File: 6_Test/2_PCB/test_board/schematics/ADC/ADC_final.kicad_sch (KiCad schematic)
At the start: 19 parts, among them J3 TSW-107-07-F-D, J4 TSW-107-07-F-D

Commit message: Edits 112524
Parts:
- removed J?: 6130XX21121_61302021121, 6130XX21121_61302021121:61302021121, symbol 2x10Header:6130XX21121_61302021121
- removed R30, R31, R32, R33, R34: 1k, symbol Device:R_US
- added C11, C13, C15: 4.7u, Cap4.7uFFootprints:CAP_0603_CL10A_1P6XP8_SAM, symbol Device:C
- added C12, C14, C16: 100n, cap100nFFootprints:CAP_CL05_SAM, symbol Device:C
- added J10: Chip_AVSS_GND_Jumpers, ECE628_lib:6x2header, symbol 6x2Header:TSW-107-07-F-D
- added J5: Chip_VDD_Jumpers, Connector_PinHeader_2.54mm:PinHeader_2x03_P2.54mm_Vertical, symbol Connector_Generic:Conn_02x03_Odd_Even
- added R11, R12, R13, R14, R15: 1k, resistor1kFootprints:RC0402N_YAG, symbol Device:R_US
- ADC2: value ~ -> ADC_Socket; footprint Package_DFN_QFN:QFN-32-1EP_5x5mm_P0.5mm_EP3.1x3.1mm_ThermalVias -> Package_DIP:DIP-32_W15.24mm_Socket
- ADC?: value ~ -> ADC_Chip
- C17: renamed from C13; footprint (none) -> cap100pFFootprints:G-033_MUR
- C18: renamed from C14; footprint (none) -> cap100pFFootprints:G-033_MUR
- C19: renamed from C15; footprint (none) -> cap100pFFootprints:G-033_MUR
- C20: renamed from C16; footprint (none) -> cap100pFFootprints:G-033_MUR
- C21: renamed from C17; footprint (none) -> cap100pFFootprints:G-033_MUR
- C22: renamed from C18; footprint (none) -> cap100pFFootprints:G-033_MUR
- J6: renamed from J?; value ~ -> BNC_Odd; footprint (none) -> ECE628_lib:bnc_mini_gnd
- J7: renamed from J?; value ~ -> BNC_Even; footprint (none) -> ECE628_lib:bnc_mini_gnd
- J8: renamed from J3; value TSW-107-07-F-D -> BNC_Jumpers
- J9: renamed from J4; value TSW-107-07-F-D -> Analog_Input_Jumpers
- R10: renamed from R29; footprint (none) -> resistor1kFootprints:RC0402N_YAG
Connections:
- net AVSS: now also J10.1, J10.2, J10.3
- net GND: now also C11.2, C12.2, C13.2, C14.2, C15.2, C16.2, J10.12, J10.4, J10.5, J10.6
- net IN2: now also R11.1
- net IN3: now also R12.1
- net IN4: now also R13.1
- net IN5: now also R14.1
- net IN6: now also R15.1
- net IOVDD: now also J5.3 (Pin_3), J5.5 (Pin_5)
- net VDD: now also J5.1 (Pin_1)
- net at ADC2.7 (IN5), ADC?.7 (IN5), C21.1: now also R14.2
- net at ADC2.2 (IN2), ADC?.2 (IN2), C18.1: now also R11.2
- net at ADC2.6 (IN4), ADC?.6 (IN4), C20.1: now also R13.2
- net at ADC2.8 (IN6), ADC?.8 (IN6), C22.1: now also R15.2
- net at ADC2.12 (IOVSS), ADC?.12 (IOVSS): now also J10.11
- net at ADC2.20 (IOVSS), ADC?.20 (IOVSS): now also J10.9
- net at ADC2.16 (VSS), ADC?.16 (VSS): now also J10.10
- net at ADC2.21 (IOVDD), ADC?.21 (IOVDD): now also C13.1, C14.1, J5.4 (Pin_4)
- net at ADC2.29 (IOVDD), ADC?.29 (IOVDD): now also C15.1, C16.1, J5.6 (Pin_6)
- net at ADC2.10 (AVSS), ADC?.10 (AVSS): now also J10.13
- net at ADC2.9 (PAD), ADC?.9 (PAD): now also J10.14
- net at ADC2.25 (VDD), ADC?.25 (VDD): now also C11.1, C12.1, J5.2 (Pin_2)
- net at ADC2.3 (IN3), ADC?.3 (IN3), C19.1: now also R12.2
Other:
- moved on the sheet: ADC2, ADC?, C17, C18, C19, C20, C21, C22, J6, J7, J8, J9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

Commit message: final draft of board, revision 2
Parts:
- removed J10: Chip_AVSS_GND_Jumpers, ECE628_lib:6x2header, symbol 6x2Header:TSW-107-07-F-D
- removed J5: Chip_VDD_Jumpers, Connector_PinHeader_2.54mm:PinHeader_2x03_P2.54mm_Vertical, symbol Connector_Generic:Conn_02x03_Odd_Even
- removed J8: BNC_Jumpers, TSW-107-07-G-D_SAI, symbol 6x2Header:TSW-107-07-F-D
- removed J9: Analog_Input_Jumpers, TSW-107-07-G-D_SAI, symbol 6x2Header:TSW-107-07-F-D
- added J10: Chip_AVSS_GND_Jumpers, CONN_713080000-SD_12_M6p10_MOL, symbol 2x6Header:15910120
- added J5: Chip_VDD_Jumpers, CONN6_M20-8760342_HRW, symbol 2x3Header:M20-8760342
- added J8: BNC_Jumpers, CONN_713080000-SD_12_M6p10_MOL, symbol 2x6Header:15910120
- added J9: Analog_Input_Jumpers, CONN_713080000-SD_12_M6p10_MOL, symbol 2x6Header:15910120
- C11, C13, C15: footprint Cap4.7uFFootprints:CAP_0603_CL10A_1P6XP8_SAM -> Capacitor_SMD:C_0603_1608Metric
- C12, C14, C16: footprint cap100nFFootprints:CAP_CL05_SAM -> Capacitor_SMD:C_0402_1005Metric
- C17, C18, C19, C20, C21, C22: footprint cap100pFFootprints:G-033_MUR -> Capacitor_SMD:C_0201_0603Metric
- R10, R11, R12, R13, R14, R15: footprint resistor1kFootprints:RC0402N_YAG -> Resistor_SMD:R_0402_1005Metric
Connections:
- net AVSS: now also J10.A1, J10.A2, J10.A3, J9.B1, J9.B2, J9.B3, J9.B4, J9.B5, J9.B6
- net GND: now also J10.A4, J10.A5, J10.A6, J10.B3
- net IN1: now also J8.B1, J9.A1
- net IN2: now also J8.B2, J9.A2
- net IN3: now also J8.B3, J9.A3
- net IN4: now also J8.B4, J9.A4
- net IN5: now also J8.B5, J9.A5
- net IN6: now also J8.B6, J9.A6
- net IOVDD: now also J5.1, J5.2
- net VDD: now also J5.3
- net at ADC2.25 (VDD), ADC?.25 (VDD), C11.1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: now also J5.6
- net at ADC2.21 (IOVDD), ADC?.21 (IOVDD), C13.1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: now also J5.5
- net at ADC2.29 (IOVDD), ADC?.29 (IOVDD), C15.1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: now also J5.4
- net at J6.1 (Signal): now also J8.A1, J8.A3, J8.A5
- net at ADC2.16 (VSS), ADC?.16 (VSS): now also J10.B5
- net at ADC2.12 (IOVSS), ADC?.12 (IOVSS): now also J10.B4
- net at ADC2.10 (AVSS), ADC?.10 (AVSS): now also J10.B2
- net at ADC2.9 (PAD), ADC?.9 (PAD): now also J10.B1
- net at ADC2.20 (IOVSS), ADC?.20 (IOVSS): now also J10.B6
- net at J7.1 (Signal): now also J8.A2, J8.A4, J8.A6

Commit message: DRC passing with all our components and pcbway rules
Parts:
- ADC?: footprint Package_DFN_QFN:QFN-32-1EP_5x5mm_P0.5mm_EP3.1x3.1mm_ThermalVias -> Package_DFN_QFN:QFN-32-1EP_5x5mm_P0.5mm_EP3.6x3.6mm
- J10, J8, J9: footprint CONN_713080000-SD_12_M6p10_MOL -> ECE628_lib:2x6Header
- J5: footprint CONN6_M20-8760342_HRW -> ECE628_lib:2x3Header
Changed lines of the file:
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@@
 			)
 		)
-		(property "Footprint" "CONN_713080000-SD_12_M6p10_MOL"
+		(property "Footprint" "ECE628_lib:2x6Header"
 			(at 106.68 119.38 0)
 			(effects
@@
 			)
 		)
-		(property "Footprint" "CONN_713080000-SD_12_M6p10_MOL"
+		(property "Footprint" "ECE628_lib:2x6Header"
 			(at 134.62 207.01 0)
 			(effects
@@
 			)
 		)
-		(property "Footprint" "CONN_713080000-SD_12_M6p10_MOL"
+		(property "Footprint" "ECE628_lib:2x6Header"
 			(at 69.85 205.74 0)
 			(effects
@@
 			)
 		)
-		(property "Footprint" "Package_DFN_QFN:QFN-32-1EP_5x5mm_P0.5mm_EP3.1x3.1mm_ThermalVias"
+		(property "Footprint" "Package_DFN_QFN:QFN-32-1EP_5x5mm_P0.5mm_EP3.6x3.6mm"
 			(at 229.87 151.13 0)
 			(effects
@@
 			)
 		)
-		(property "Footprint" "CONN6_M20-8760342_HRW"
+		(property "Footprint" "ECE628_lib:2x3Header"
 			(at 73.66 25.4 0)
 			(effects

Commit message: Edit Layout 1_27
Rearranged the components in the layout and added majority of traces and ground layer. AVSS connections still need to be connected along with IOVDD
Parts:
- J10, J8, J9: footprint ECE628_lib:2x6Header -> Connector_PinHeader_2.54mm:PinHeader_2x06_P2.54mm_Vertical
- J5: footprint ECE628_lib:2x3Header -> Connector_PinHeader_2.54mm:PinHeader_2x03_P2.54mm_Vertical
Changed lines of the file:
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@@
 			)
 		)
-		(property "Footprint" "ECE628_lib:2x6Header"
+		(property "Footprint" "Connector_PinHeader_2.54mm:PinHeader_2x06_P2.54mm_Vertical"
 			(at 106.68 119.38 0)
 			(effects
@@
 			)
 		)
-		(property "Footprint" "ECE628_lib:2x6Header"
+		(property "Footprint" "Connector_PinHeader_2.54mm:PinHeader_2x06_P2.54mm_Vertical"
 			(at 134.62 207.01 0)
 			(effects
@@
 			)
 		)
-		(property "Footprint" "ECE628_lib:2x6Header"
+		(property "Footprint" "Connector_PinHeader_2.54mm:PinHeader_2x06_P2.54mm_Vertical"
 			(at 69.85 205.74 0)
 			(effects
@@
 			)
 		)
-		(property "Footprint" "ECE628_lib:2x3Header"
+		(property "Footprint" "Connector_PinHeader_2.54mm:PinHeader_2x03_P2.54mm_Vertical"
 			(at 73.66 25.4 0)
 			(effects

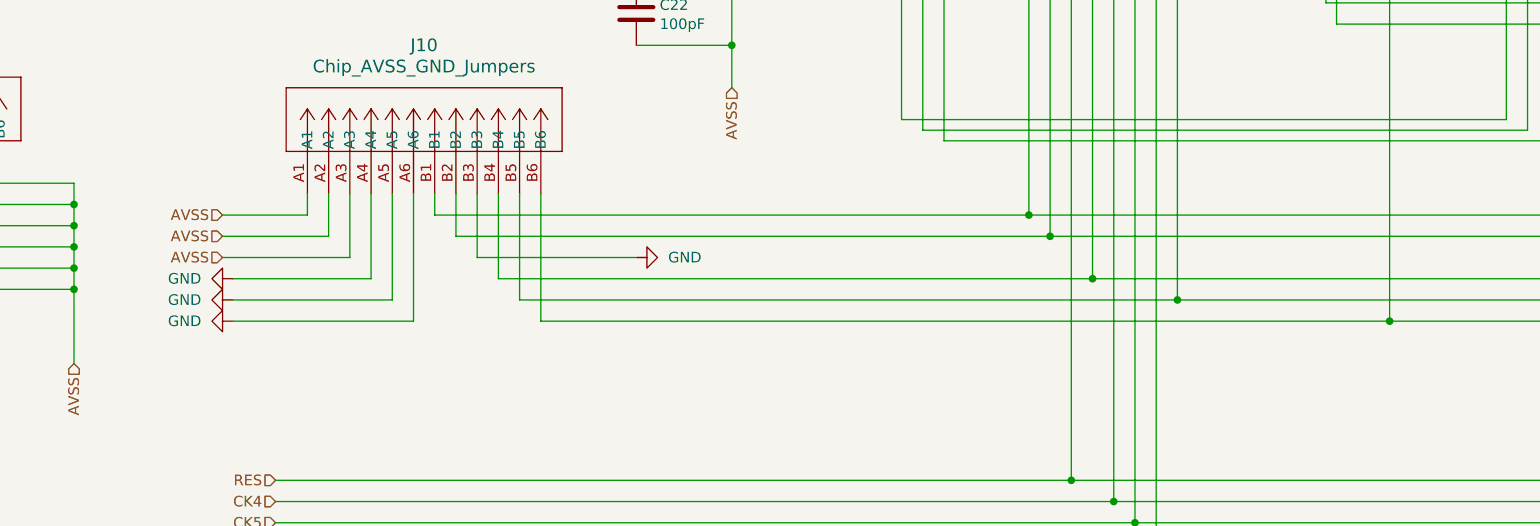
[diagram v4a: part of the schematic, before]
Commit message: Fixed DRC errors
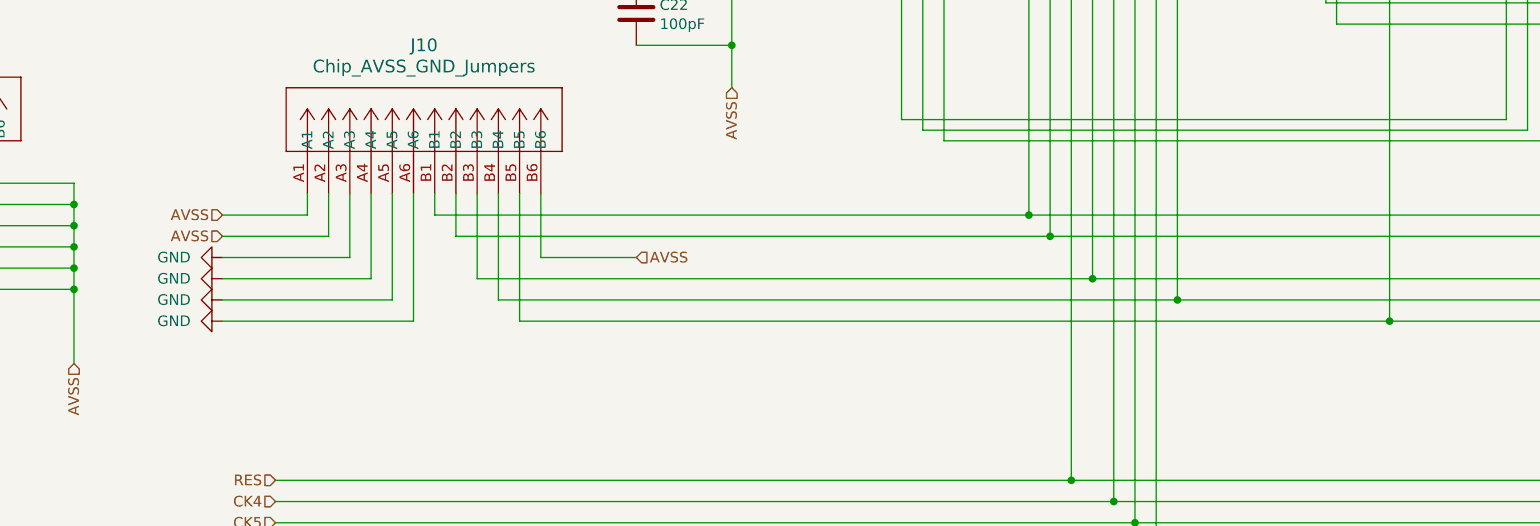
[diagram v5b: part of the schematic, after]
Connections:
- net AVSS: now also J10.B6; no longer J10.A3
- net GND: now also J10.A3; no longer J10.B3
- net at ADC2.12 (IOVSS), ADC?.12 (IOVSS): now also J10.B3; no longer J10.B4
- net at ADC2.16 (VSS), ADC?.16 (VSS): now also J10.B4; no longer J10.B5
- net at ADC2.20 (IOVSS), ADC?.20 (IOVSS): now also J10.B5; no longer J10.B6

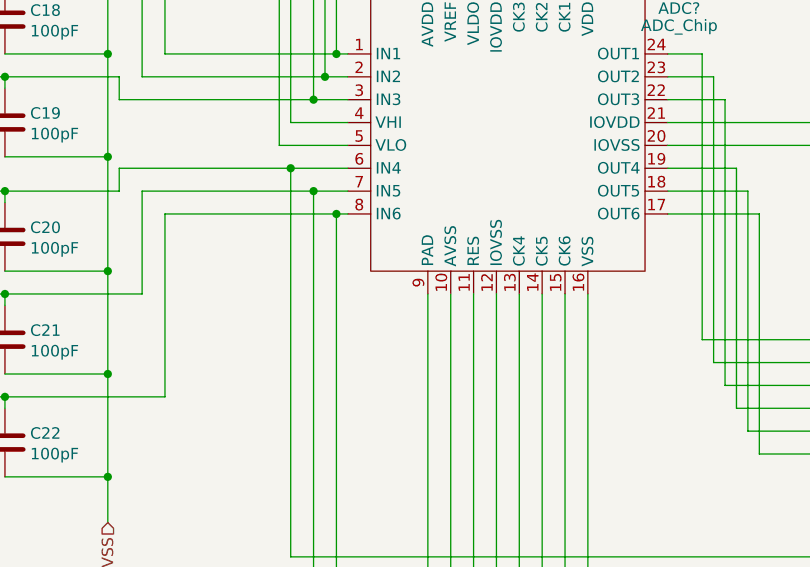
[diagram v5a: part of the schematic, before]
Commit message: Board Edits 250206
- Added the terminal block (4 positions - VSUP, GND, GND, & AVSS)
- Added vias for test points
- Added silkscreen labels for all inputs, jumpers, and potentiometers
- Widened traces going across the board
- Relabeled plane as AVSS plane
- Fixes to 3D model of board
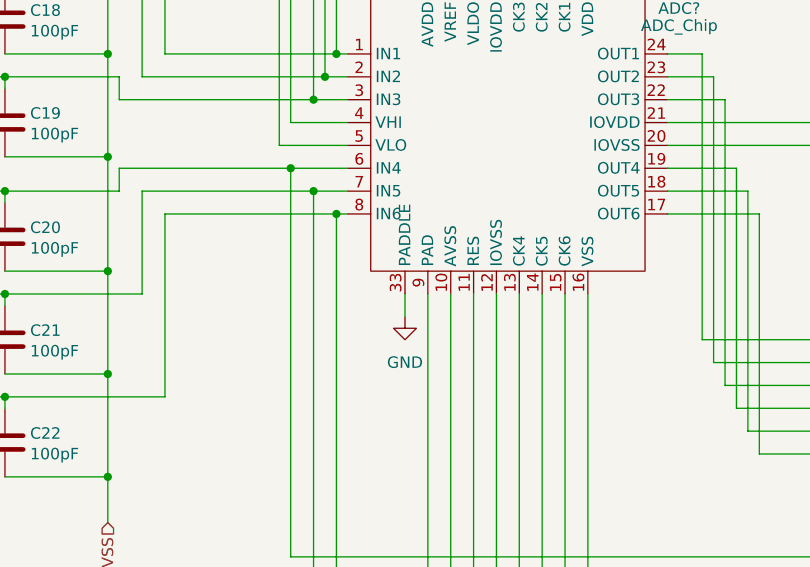
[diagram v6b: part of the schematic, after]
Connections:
- net GND: now also ADC?.33 (PADDLE)
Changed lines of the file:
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@@
+	(wire
+		(pts
+			(xy 218.44 168.91) (xy 218.44 171.45)
+		)
+		(stroke
+			(width 0)
+			(type default)
+		)
+	)
 	(wire
 		(pts
@@
 	)
 	(symbol
+		(lib_name "Chip_1")
 		(lib_id "ADC:Chip")
 		(at 229.87 151.13 0)
@@
 		)
 		(pin "11"
+		)
+		(pin "33"
 		)
 		(instances
@@
 					(unit 1)
 				)
+			)
+		)
+	)
+	(symbol
+		(lib_id "power:GND")
+		(at 218.44 171.45 0)
+		(unit 1)
+		(exclude_from_sim no)
+		(in_bom yes)
+		(on_board yes)
+		(dnp no)
+		(fields_autoplaced yes)
+		(property "Reference" "#PWR028"
+			(at 218.44 177.8 0)
+			(effects
+				(font
+					(size 1.27 1.27)
+				)
+				(hide yes)
+			)
+		)
+		(property "Value" "GND"
+			(at 218.44 176.53 0)
+			(effects
+				(font
+					(size 1.27 1.27)
+				)
+			)
+		)
+		(property "Footprint" ""
+			(at 218.44 171.45 0)
+			(effects
+				(font
+					(size 1.27 1.27)
+				)
+				(hide yes)
+			)
+		)
+		(property "Datasheet" ""
+			(at 218.44 171.45 0)
+			(effects
+				(font
+					(size 1.27 1.27)
+				)
+				(hide yes)
+			)
+		)
+		(property "Description" "Power symbol creates a global label with name \"GND\" , ground"
+			(at 218.44 171.45 0)
+			(effects
+				(font
+					(size 1.27 1.27)
+				)
+				(hide yes)
+			)
+		)
+		(pin "1"
+		)
+		(instances
+			(project ""
+				(path "/9c0580c5-7bd5-4e54-bf4c-826aa4ac3630/26226914-76fb-4db0-a074-5233062a7d0a"
+					(reference "#PWR028")
+					(unit 1)
+				)
